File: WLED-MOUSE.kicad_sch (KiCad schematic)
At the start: 2 parts

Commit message: added some parts, symbols and fooprints for a few things. allso 'touched grass' as this was recomended by a frined who said i was working too hard in linux. :3
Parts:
- added C?: C, symbol Device:C
- added C?: 25uF, Capacitor_SMD:C_0805_2012Metric, symbol Device:C
- added J? (x2): Conn_01x03_Female, symbol Connector:Conn_01x03_Female
- added J?: Power-in, symbol Connector:Conn_01x02_Female
- added J?: FTDI-header, symbol Connector:Conn_01x06_Male
- added JP?: SolderJumper_3_Bridged12, symbol Jumper:SolderJumper_3_Bridged12
- added R?: R, symbol Device:R
- added U?: ESP32-WROOM-32D, esp32:ESP32-DEVKITC-32D, symbol RF_Module:ESP32-WROOM-32D
- J?: value Conn_01x03_Male -> Pixel-strip
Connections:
- net GND: now reaches U?.1 (GND), U?.15 (GND), U?.38 (GND), U?.39 (GND)
- net GND: now also C?.2, C?.2, J?.1 (Pin_1)
- net +3.3V: now reaches U?.2 (VDD)
- net +3.3V: now also C?.1, JP?.1 (A), R?.1
- net GPIO-0: now reaches U?.25 (IO0)
- net GPIO-0: now also J?.2 (Pin_2)
- net Reset: now reaches U?.3 (EN)
- net Reset: now also C?.1, J?.6 (Pin_6), R?.2
- net Rx: now reaches U?.34 (RXD0/IO3)
- net Tx: now reaches U?.35 (TXD0/IO1)
- new net: J?.3 (Pin_3), JP?.2 (C)
- new net: U?.1 (GND), U?.15 (GND), U?.38 (GND), U?.39 (GND)
- new net +5V: JP?.3 (B)
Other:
- note added: "Reset Circuitry."
- note added: "change symbol pinout / fork it https://dl.espressif.com/dl/schematics/esp32_devkitc_v4-sch.pdf"
- note added: "i2s mic ( INMP441 )"
- note removed: "i2s mic"

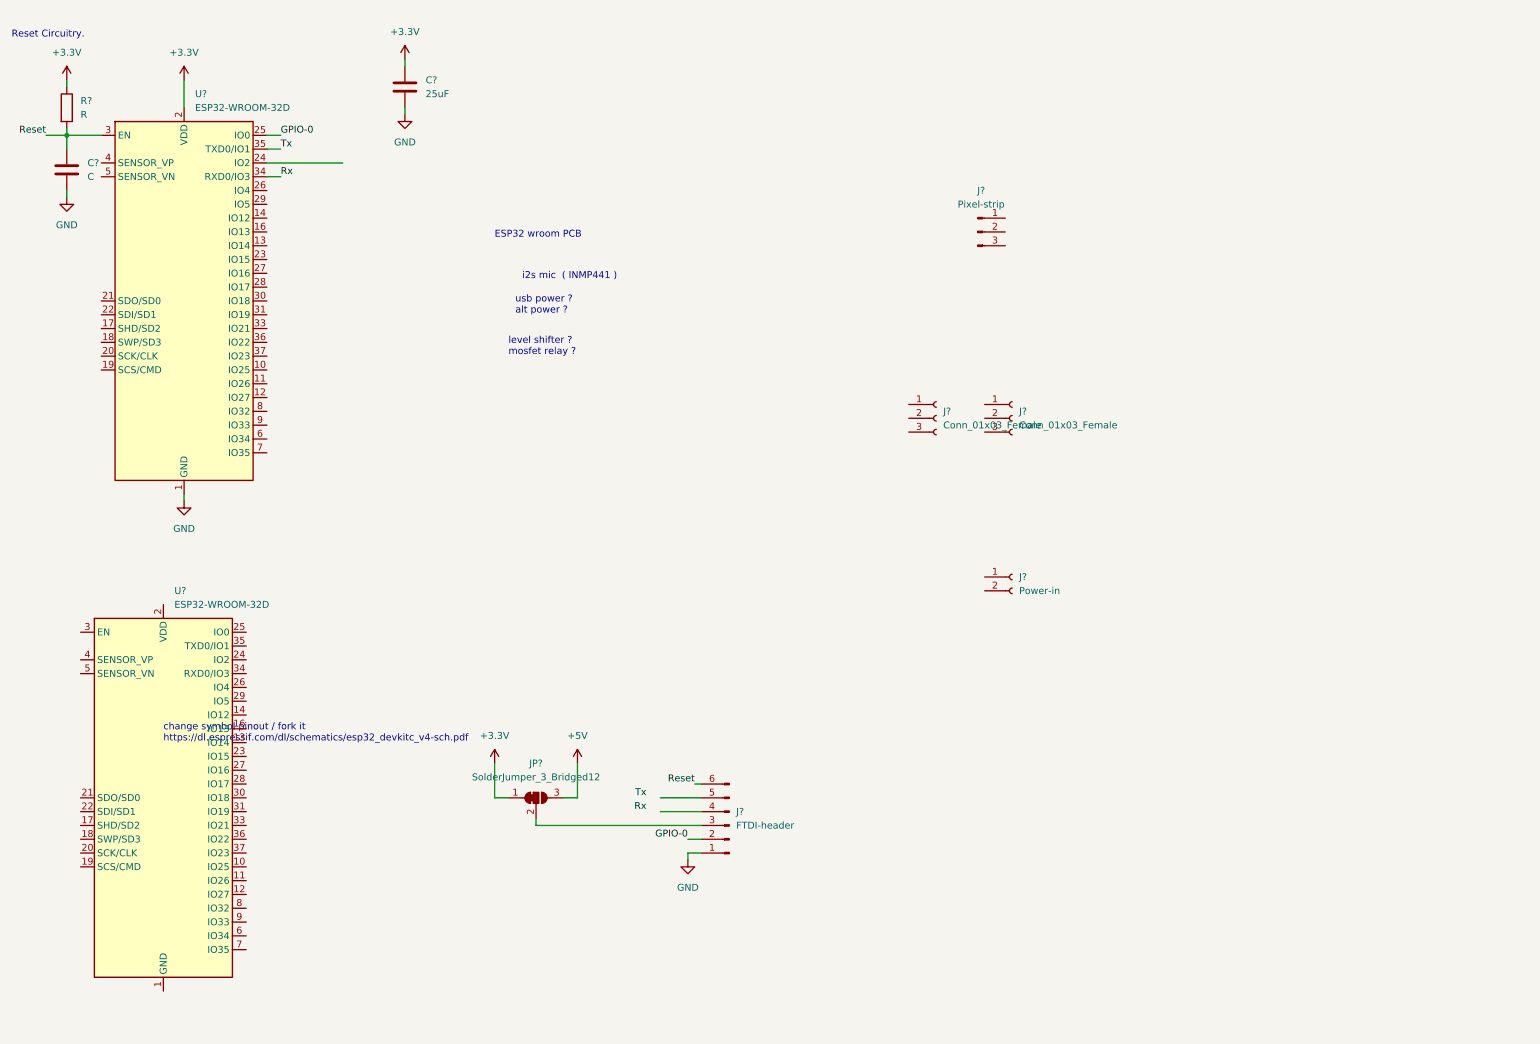
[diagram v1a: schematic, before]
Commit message: added some footprints for components
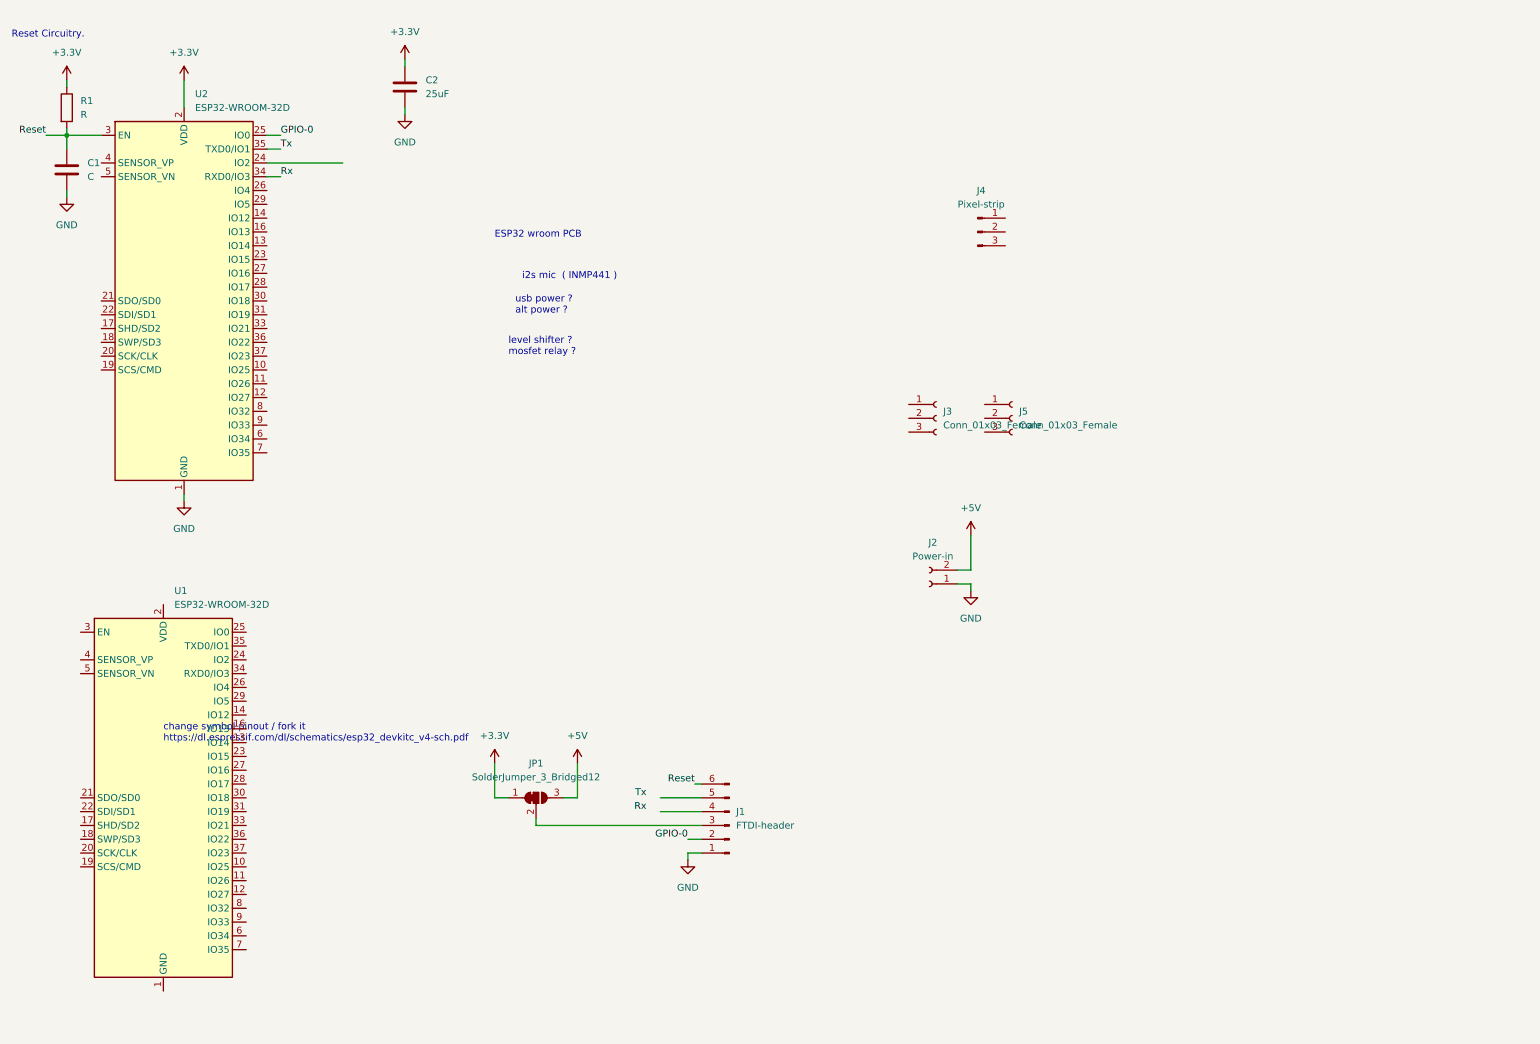
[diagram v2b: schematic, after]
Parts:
- C1: renamed from C?; footprint (none) -> Capacitor_SMD:C_0805_2012Metric
- J1: renamed from J?; footprint (none) -> Connector_PinSocket_2.54mm:PinSocket_1x06_P2.54mm_Vertical
- J2: renamed from J?; footprint (none) -> TerminalBlock:TerminalBlock_Altech_AK300-2_P5.00mm
- J4: renamed from J?; footprint (none) -> Connector_PinSocket_2.54mm:PinSocket_1x03_P2.54mm_Vertical
- JP1: renamed from JP?; footprint (none) -> Jumper:SolderJumper-3_P1.3mm_Open_RoundedPad1.0x1.5mm
- R1: renamed from R?; footprint (none) -> Resistor_SMD:R_0603_1608Metric
- gave numbers to parts that had none: 5
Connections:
- net +5V: now also J2.2 (Pin_2)
- net GND: now also J2.1 (Pin_1)
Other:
- moved on the sheet: J2

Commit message: added some more nice little bits
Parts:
- added J6, J7, J8: Pixel-strip, Connector_PinSocket_2.54mm:PinSocket_1x03_P2.54mm_Vertical, symbol Connector:Conn_01x03_Male
- added U3: SN74LV4T125, Package_SO:TSSOP-14_4.4x5mm_P0.65mm, symbol 74xx:SN74LV4T125
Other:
- moved on the sheet: J4
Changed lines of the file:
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@@
     (effects (font (size 1.27 1.27)) (justify right bottom))
+  )
+  (symbol (lib_id "74xx:SN74LV4T125") (at 214.63 41.91 0) (unit 5)
+    (in_bom yes) (on_board yes) (fields_autoplaced)
+    (property "Reference" "U3" (id 0) (at 220.98 40.6399 0)
+      (effects (font (size 1.27 1.27)) (justify left))
+    )
+    (property "Value" "SN74LV4T125" (id 1) (at 220.98 43.1799 0)
+      (effects (font (size 1.27 1.27)) (justify left))
+    )
+    (property "Footprint" "Package_SO:TSSOP-14_4.4x5mm_P0.65mm" (id 2) (at 214.63 41.91 0)
+      (effects (font (size 1.27 1.27)) hide)
+    )
+    (property "Datasheet" "https://www.ti.com/lit/ds/symlink/sn74lv4t125.pdf" (id 3) (at 214.63 41.91 0)
+      (effects (font (size 1.27 1.27)) hide)
+    )
+    (pin "1")
+    (pin "2")
+    (pin "3")
+    (pin "4")
+    (pin "5")
+    (pin "6")
+    (pin "10")
+    (pin "8")
+    (pin "9")
+    (pin "11")
+    (pin "12")
+    (pin "13")
+    (pin "14")
+    (pin "7")
+  )
+  (symbol (lib_id "Connector:Conn_01x03_Male") (at 193.04 21.59 0) (unit 1)
+    (in_bom yes) (on_board yes) (fields_autoplaced)
+    (property "Reference" "J6" (id 0) (at 193.675 13.97 0))
+    (property "Value" "Pixel-strip" (id 1) (at 193.675 16.51 0))
+    (property "Footprint" "Connector_PinSocket_2.54mm:PinSocket_1x03_P2.54mm_Vertical" (id 2) (at 193.04 21.59 0)
+      (effects (font (size 1.27 1.27)) hide)
+    )
+    (property "Datasheet" "~" (id 3) (at 193.04 21.59 0)
+      (effects (font (size 1.27 1.27)) hide)
+    )
+    (pin "1")
+    (pin "2")
+    (pin "3")
+  )
+  (symbol (lib_id "Connector:Conn_01x03_Male") (at 193.04 48.26 0) (unit 1)
+    (in_bom yes) (on_board yes) (fields_autoplaced)
+    (property "Reference" "J7" (id 0) (at 193.675 40.64 0))
+    (property "Value" "Pixel-strip" (id 1) (at 193.675 43.18 0))
+    (property "Footprint" "Connector_PinSocket_2.54mm:PinSocket_1x03_P2.54mm_Vertical" (id 2) (at 193.04 48.26 0)
+      (effects (font (size 1.27 1.27)) hide)
+    )
+    (property "Datasheet" "~" (id 3) (at 193.04 48.26 0)
+      (effects (font (size 1.27 1.27)) hide)
+    )
+    (pin "1")
+    (pin "2")
+    (pin "3")
   )
   (symbol (lib_id "power:+3.3V") (at 91.44 21.59 0) (unit 1)
@@
     )
     (pin "1")
+  )
+  (symbol (lib_id "74xx:SN74LV4T125") (at 148.59 52.07 0) (unit 4)
+    (in_bom yes) (on_board yes) (fields_autoplaced)
+    (property "Reference" "U3" (id 0) (at 148.59 43.18 0))
+    (property "Value" "SN74LV4T125" (id 1) (at 148.59 45.72 0))
+    (property "Footprint" "Package_SO:TSSOP-14_4.4x5mm_P0.65mm" (id 2) (at 148.59 52.07 0)
+      (effects (font (size 1.27 1.27)) hide)
+    )
+    (property "Datasheet" "https://www.ti.com/lit/ds/symlink/sn74lv4t125.pdf" (id 3) (at 148.59 52.07 0)
+      (effects (font (size 1.27 1.27)) hide)
+    )
+    (pin "1")
+    (pin "2")
+    (pin "3")
+    (pin "4")
+    (pin "5")
+    (pin "6")
+    (pin "10")
+    (pin "8")
+    (pin "9")
+    (pin "11")
+    (pin "12")
+    (pin "13")
+    (pin "14")
+    (pin "7")
   )
   (symbol (lib_id "Connector:Conn_01x03_Female") (at 203.2 87.63 0) (unit 1)
@@
     )
     (property "Datasheet" "~" (id 3) (at 115.57 157.48 0)
+      (effects (font (size 1.27 1.27)) hide)
+    )
+    (pin "1")
+    (pin "2")
+    (pin "3")
+  )
+  (symbol (lib_id "Connector:Conn_01x03_Male") (at 194.31 60.96 0) (unit 1)
+    (in_bom yes) (on_board yes) (fields_autoplaced)
+    (property "Reference" "J8" (id 0) (at 194.945 53.34 0))
+    (property "Value" "Pixel-strip" (id 1) (at 194.945 55.88 0))
+    (property "Footprint" "Connector_PinSocket_2.54mm:PinSocket_1x03_P2.54mm_Vertical" (id 2) (at 194.31 60.96 0)
+      (effects (font (size 1.27 1.27)) hide)
+    )
+    (property "Datasheet" "~" (id 3) (at 194.31 60.96 0)
       (effects (font (size 1.27 1.27)) hide)
     )
@@
     (pin "2")
   )
+  (symbol (lib_id "74xx:SN74LV4T125") (at 170.18 33.02 0) (unit 1)
+    (in_bom yes) (on_board yes) (fields_autoplaced)
+    (property "Reference" "U3" (id 0) (at 170.18 24.13 0))
+    (property "Value" "SN74LV4T125" (id 1) (at 170.18 26.67 0))
+    (property "Footprint" "Package_SO:TSSOP-14_4.4x5mm_P0.65mm" (id 2) (at 170.18 33.02 0)
+      (effects (font (size 1.27 1.27)) hide)
+    )
+    (property "Datasheet" "https://www.ti.com/lit/ds/symlink/sn74lv4t125.pdf" (id 3) (at 170.18 33.02 0)
+      (effects (font (size 1.27 1.27)) hide)
+    )
+    (pin "1")
+    (pin "2")
+    (pin "3")
+    (pin "4")
+    (pin "5")
+    (pin "6")
+    (pin "10")
+    (pin "8")
+    (pin "9")
+    (pin "11")
+    (pin "12")
+    (pin "13")
+    (pin "14")
+    (pin "7")
+  )
   (symbol (lib_id "power:+3.3V") (at 50.8 25.4 0) (unit 1)
     (in_bom yes) (on_board yes) (fields_autoplaced)
@@
     (pin "3")
   )
-  (symbol (lib_id "Connector:Conn_01x03_Male") (at 196.85 53.34 0) (unit 1)
-    (in_bom yes) (on_board yes) (fields_autoplaced)
-    (property "Reference" "J4" (id 0) (at 197.485 45.72 0))
-    (property "Value" "Pixel-strip" (id 1) (at 197.485 48.26 0))
-    (property "Footprint" "Connector_PinSocket_2.54mm:PinSocket_1x03_P2.54mm_Vertical" (id 2) (at 196.85 53.34 0)
-      (effects (font (size 1.27 1.27)) hide)
-    )
-    (property "Datasheet" "~" (id 3) (at 196.85 53.34 0)
-      (effects (font (size 1.27 1.27)) hide)
-    )
-    (pin "1")
-    (pin "2")
-    (pin "3")
+  (symbol (lib_id "Connector:Conn_01x03_Male") (at 193.04 33.02 0) (unit 1)
+    (in_bom yes) (on_board yes) (fields_autoplaced)
+    (property "Reference" "J4" (id 0) (at 193.675 25.4 0))
+    (property "Value" "Pixel-strip" (id 1) (at 193.675 27.94 0))
+    (property "Footprint" "Connector_PinSocket_2.54mm:PinSocket_1x03_P2.54mm_Vertical" (id 2) (at 193.04 33.02 0)
+      (effects (font (size 1.27 1.27)) hide)
+    )
+    (property "Datasheet" "~" (id 3) (at 193.04 33.02 0)
+      (effects (font (size 1.27 1.27)) hide)
+    )
+    (pin "1")
+    (pin "2")
+    (pin "3")
+  )
+  (symbol (lib_id "74xx:SN74LV4T125") (at 170.18 52.07 0) (unit 2)
+    (in_bom yes) (on_board yes) (fields_autoplaced)
+    (property "Reference" "U3" (id 0) (at 170.18 43.18 0))
+    (property "Value" "SN74LV4T125" (id 1) (at 170.18 45.72 0))
+    (property "Footprint" "Package_SO:TSSOP-14_4.4x5mm_P0.65mm" (id 2) (at 170.18 52.07 0)
+      (effects (font (size 1.27 1.27)) hide)
+    )
+    (property "Datasheet" "https://www.ti.com/lit/ds/symlink/sn74lv4t125.pdf" (id 3) (at 170.18 52.07 0)
+      (effects (font (size 1.27 1.27)) hide)
+    )
+    (pin "1")
+    (pin "2")
+    (pin "3")
+    (pin "4")
+    (pin "5")
+    (pin "6")
+    (pin "10")
+    (pin "8")
+    (pin "9")
+    (pin "11")
+    (pin "12")
+    (pin "13")
+    (pin "14")
+    (pin "7")
   )
   (symbol (lib_id "RF_Module:ESP32-WROOM-32D") (at 50.8 66.04 0) (unit 1)
@@
     (pin "2")
   )
+  (symbol (lib_id "74xx:SN74LV4T125") (at 148.59 33.02 0) (unit 3)
+    (in_bom yes) (on_board yes) (fields_autoplaced)
+    (property "Reference" "U3" (id 0) (at 148.59 24.13 0))
+    (property "Value" "SN74LV4T125" (id 1) (at 148.59 26.67 0))
+    (property "Footprint" "Package_SO:TSSOP-14_4.4x5mm_P0.65mm" (id 2) (at 148.59 33.02 0)
+      (effects (font (size 1.27 1.27)) hide)
+    )
+    (property "Datasheet" "https://www.ti.com/lit/ds/symlink/sn74lv4t125.pdf" (id 3) (at 148.59 33.02 0)
+      (effects (font (size 1.27 1.27)) hide)
+    )
+    (pin "1")
+    (pin "2")
+    (pin "3")
+    (pin "4")
+    (pin "5")
+    (pin "6")
+    (pin "10")
+    (pin "8")
+    (pin "9")
+    (pin "11")
+    (pin "12")
+    (pin "13")
+    (pin "14")
+    (pin "7")
+  )
   (symbol (lib_id "power:GND") (at 50.8 102.87 0) (unit 1)
     (in_bom yes) (on_board yes) (fields_autoplaced)
@@
       (reference "J5") (unit 1) (value "Conn_01x03_Female") (footprint "")
     )
+    (path "/2147e67f-9bcc-4308-b668-83ebdc248d3d"
+      (reference "J6") (unit 1) (value "Pixel-strip") (footprint "Connector_PinSocket_2.54mm:PinSocket_1x03_P2.54mm_Vertical")
+    )
+    (path "/2652f8a8-3595-4675-a853-7412d93bdd21"
+      (reference "J7") (unit 1) (value "Pixel-strip") (footprint "Connector_PinSocket_2.54mm:PinSocket_1x03_P2.54mm_Vertical")
+    )
+    (path "/6080e04b-25a1-46fc-8d59-8e226e075c93"
+      (reference "J8") (unit 1) (value "Pixel-strip") (footprint "Connector_PinSocket_2.54mm:PinSocket_1x03_P2.54mm_Vertical")
+    )
     (path "/50b66b8a-e326-4fb2-9fa5-ac5ec73de766"
       (reference "JP1") (unit 1) (value "SolderJumper_3_Bridged12") (footprint "Jumper:SolderJumper-3_P1.3mm_Open_RoundedPad1.0x1.5mm")
@@
       (reference "U2") (unit 1) (value "ESP32-WROOM-32D") (footprint "RF_Module:ESP32-WROOM-32")
     )
-  )
+    (path "/8c42deb5-0c65-4966-a80a-31aaca38674c"
+      (reference "U3") (unit 1) (value "SN74LV4T125") (footprint "Package_SO:TSSOP-14_4.4x5mm_P0.65mm")
+    )
+    (path "/b58ad889-2b4f-400f-b0ab-f7075892088d"
+      (reference "U3") (unit 2) (value "SN74LV4T125") (footprint "Package_SO:TSSOP-14_4.4x5mm_P0.65mm")
+    )
+    (path "/ebe613f3-86be-431e-b571-7d5a30b5cb5a"
+      (reference "U3") (unit 3) (value "SN74LV4T125") (footprint "Package_SO:TSSOP-14_4.4x5mm_P0.65mm")
+    )
+    (path "/350e1a2e-7508-44a6-af56-cb96be92c94c"
+      (reference "U3") (unit 4) (value "SN74LV4T125") (footprint "Package_SO:TSSOP-14_4.4x5mm_P0.65mm")
+    )
+    (path "/079cf57b-15d2-4bbd-aaf4-f04e01af667f"
+      (reference "U3") (unit 5) (value "SN74LV4T125") (footprint "Package_SO:TSSOP-14_4.4x5mm_P0.65mm")
+    )
+  )
